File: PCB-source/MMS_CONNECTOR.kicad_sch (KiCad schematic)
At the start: 6 parts, among them J9 RJ45_LED_Shielded, U3 TPD2EUSB30DRTR-TP

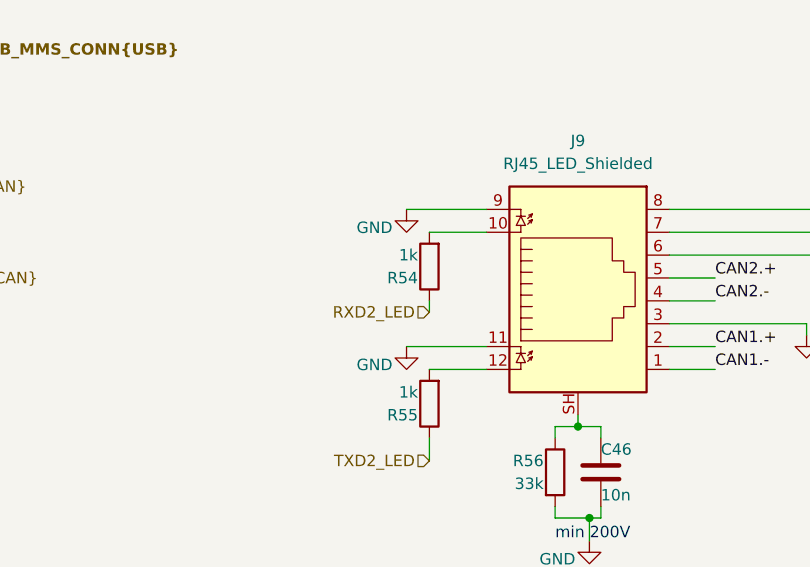
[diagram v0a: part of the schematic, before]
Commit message: change can term add usr led
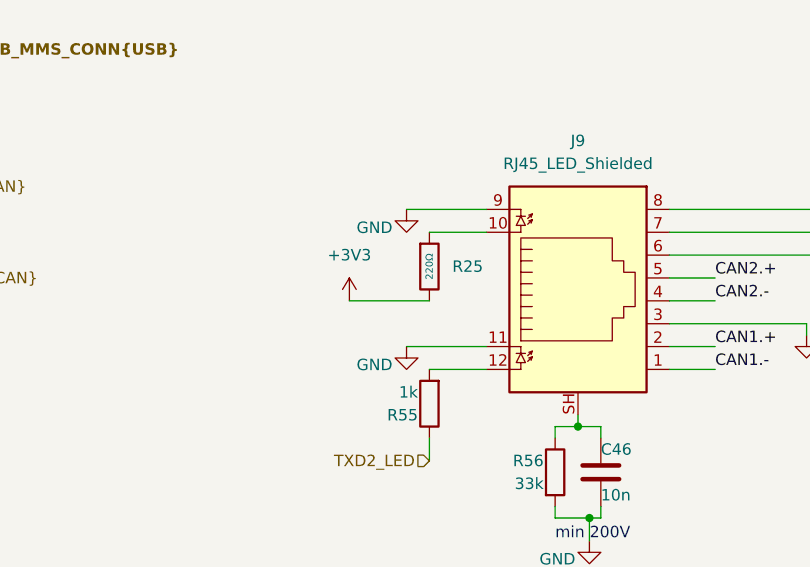
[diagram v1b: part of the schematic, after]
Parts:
- removed R54: 1k, Resistor_SMD:R_0402_1005Metric, symbol Device:R
- added R25: 220Ω, PCM_JLCPCB:R_0402, symbol PCM_JLCPCB-Resistors:0402,220Ω
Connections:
- net at J9.10: now also R25.1
- new net +3V3: R25.2

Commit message: DRC PASS, preparing bom for production
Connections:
- net +3V3 is gone; now on net TXD2_LED: R25.2
- net TXD2_LED: no longer R55.1
- new net RXD2_LED: R55.1
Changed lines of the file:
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@@
+	(wire
+		(pts
+			(xy 104.14 114.3) (xy 113.03 114.3)
+		)
+		(stroke
+			(width 0)
+			(type default)
+		)
+	)
 	(wire
 		(pts
@@
 			)
 			(justify left bottom)
-		)
-	)
-	(hierarchical_label "TXD2_LED"
-		(shape input)
-		(at 113.03 114.3 180)
-		(effects
-			(font
-				(size 1.27 1.27)
-			)
-			(justify right)
 		)
 	)
@@
 		)
 	)
+	(hierarchical_label "TXD2_LED"
+		(shape input)
+		(at 104.14 96.52 180)
+		(effects
+			(font
+				(size 1.27 1.27)
+			)
+			(justify right)
+		)
+	)
 	(hierarchical_label "CAN2{CAN}"
 		(shape bidirectional)
@@
 			)
 			(justify left)
+		)
+	)
+	(hierarchical_label "RXD2_LED"
+		(shape input)
+		(at 104.14 114.3 180)
+		(effects
+			(font
+				(size 1.27 1.27)
+			)
+			(justify right)
 		)
 	)
@@
 					(unit 1)
 				)
-			)
-		)
-	)
-	(symbol
-		(lib_id "power:+3V3")
-		(at 104.14 96.52 0)
-		(unit 1)
-		(exclude_from_sim no)
-		(in_bom yes)
-		(on_board yes)
-		(dnp no)
-		(fields_autoplaced yes)
-		(property "Reference" "#PWR084"
-			(at 104.14 100.33 0)
-			(effects
-				(font
-					(size 1.27 1.27)
-				)
-				(hide yes)
-			)
-		)
-		(property "Value" "+3V3"
-			(at 104.14 91.44 0)
-			(effects
-				(font
-					(size 1.27 1.27)
-				)
-			)
-		)
-		(property "Footprint" ""
-			(at 104.14 96.52 0)
-			(effects
-				(font
-					(size 1.27 1.27)
-				)
-				(hide yes)
-			)
-		)
-		(property "Datasheet" ""
-			(at 104.14 96.52 0)
-			(effects
-				(font
-					(size 1.27 1.27)
-				)
-				(hide yes)
-			)
-		)
-		(property "Description" "Power symbol creates a global label with name \"+3V3\""
-			(at 104.14 96.52 0)
-			(effects
-				(font
-					(size 1.27 1.27)
-				)
-				(hide yes)
-			)
-		)
-		(pin "1"
-		)
-		(instances
-			(project ""
-				(path "/6596548a-44e0-46d8-8624-fd71cf4a3e17/375a4799-1237-4cf9-80bd-b6d6bc52fffa"
-					(reference "#PWR085")
-					(unit 1)
-				)
-				(path "/6596548a-44e0-46d8-8624-fd71cf4a3e17/6dbf7263-2614-4625-a960-703f6ff0d778"
-					(reference "#PWR084")
-					(unit 1)
-				)

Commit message: bom done
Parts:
- removed C46: 10n, Capacitor_SMD:C_0402_1005Metric, symbol Device:C
- removed R55: 1k, Resistor_SMD:R_0402_1005Metric, symbol Device:R
- removed R56: 33k, Resistor_SMD:R_0402_1005Metric, symbol Device:R
- added C34: 10nF, PCM_JLCPCB:C_0402, symbol PCM_JLCPCB-Capacitors:0402,10nF
- added R27: 33kΩ, PCM_JLCPCB:R_0402, symbol PCM_JLCPCB-Resistors:0402,33kΩ
- added R6: 1kΩ, PCM_JLCPCB:R_0402, symbol PCM_JLCPCB-Resistors:0402,1kΩ
- J9: now left out of the parts list
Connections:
- net GND: now also C34.2, R27.2
- net RXD2_LED: now also R6.2
- net at J9.12: now also R6.1
- net at J9.SH: now also C34.1, R27.1

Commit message: REV A production ready
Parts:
- removed R6: 1kΩ, PCM_JLCPCB:R_0402, symbol PCM_JLCPCB-Resistors:0402,1kΩ
- added R6: 220Ω, PCM_JLCPCB:R_0402, symbol PCM_JLCPCB-Resistors:0402,220Ω
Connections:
- net RXD2_LED: now also R6.2
- net at J9.12: now also R6.1
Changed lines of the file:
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@@
+	)
+	(symbol
+		(lib_id "PCM_JLCPCB-Resistors:0402,220Ω")
+		(at 113.03 107.95 0)
+		(unit 1)
+		(exclude_from_sim no)
+		(in_bom yes)
+		(on_board yes)
+		(dnp no)
+		(property "Reference" "R6"
+			(at 114.554 107.95 0)
+			(effects
+				(font
+					(size 1.27 1.27)
+				)
+				(justify left)
+			)
+		)
+		(property "Value" "220Ω"
+			(at 113.03 107.95 90)
+			(do_not_autoplace yes)
+			(effects
+				(font
+					(size 0.8 0.8)
+				)
+			)
+		)
+		(property "Footprint" "PCM_JLCPCB:R_0402"
+			(at 111.252 107.95 90)
+			(effects
+				(font
+					(size 1.27 1.27)
+				)
+				(hide yes)
+			)
+		)
+		(property "Datasheet" "https://www.lcsc.com/datasheet/lcsc_datasheet_2205311900_UNI-ROYAL-Uniroyal-Elec-0402WGF2200TCE_C25091.pdf"
+			(at 113.03 107.95 0)
+			(effects
+				(font
+					(size 1.27 1.27)
+				)
+				(hide yes)
+			)
+		)
+		(property "Description" "62.5mW Thick Film Resistors 50V ±100ppm/°C ±1% 220Ω 0402 Chip Resistor - Surface Mount ROHS"
+			(at 113.03 107.95 0)
+			(effects
+				(font
+					(size 1.27 1.27)
+				)
+				(hide yes)
+			)
+		)
+		(property "LCSC" "C25091"
+			(at 113.03 107.95 0)
+			(effects
+				(font
+					(size 1.27 1.27)
+				)
+				(hide yes)
+			)
+		)
+		(property "Stock" "617243"
+			(at 113.03 107.95 0)
+			(effects
+				(font
+					(size 1.27 1.27)
+				)
+				(hide yes)
+			)
+		)
+		(property "Price" "0.004USD"
+			(at 113.03 107.95 0)
+			(effects
+				(font
+					(size 1.27 1.27)
+				)
+				(hide yes)
+			)
+		)
+		(property "Process" "SMT"
+			(at 113.03 107.95 0)
+			(effects
+				(font
+					(size 1.27 1.27)
+				)
+				(hide yes)
+			)
+		)
+		(property "Minimum Qty" "20"
+			(at 113.03 107.95 0)
+			(effects
+				(font
+					(size 1.27 1.27)
+				)
+				(hide yes)
+			)
+		)
+		(property "Attrition Qty" "10"
+			(at 113.03 107.95 0)
+			(effects
+				(font
+					(size 1.27 1.27)
+				)
+				(hide yes)
+			)
+		)
+		(property "Class" "Basic Component"
+			(at 113.03 107.95 0)
+			(effects
+				(font
+					(size 1.27 1.27)
+				)
+				(hide yes)
+			)
+		)
+		(property "Category" "Resistors,Chip Resistor - Surface Mount"
+			(at 113.03 107.95 0)
+			(effects
+				(font
+					(size 1.27 1.27)
+				)
+				(hide yes)
+			)
+		)
+		(property "Manufacturer" "UNI-ROYAL(Uniroyal Elec)"
+			(at 113.03 107.95 0)
+			(effects
+				(font
+					(size 1.27 1.27)
+				)
+				(hide yes)
+			)
+		)
+		(property "Part" "0402WGF2200TCE"
+			(at 113.03 107.95 0)
+			(effects
+				(font
+					(size 1.27 1.27)
+				)
+				(hide yes)
+			)
+		)
+		(property "Resistance" "220Ω"
+			(at 113.03 107.95 0)
+			(effects
+				(font
+					(size 1.27 1.27)
+				)
+				(hide yes)
+			)
+		)
+		(property "Power(Watts)" "62.5mW"
+			(at 113.03 107.95 0)
+			(effects
+				(font
+					(size 1.27 1.27)
+				)
+				(hide yes)
+			)
+		)
+		(property "Type" "Thick Film Resistors"
+			(at 113.03 107.95 0)
+			(effects
+				(font
+					(size 1.27 1.27)
+				)
+				(hide yes)
+			)
+		)
+		(property "Overload Voltage (Max)" "50V"
+			(at 113.03 107.95 0)
+			(effects
+				(font
+					(size 1.27 1.27)
+				)
+				(hide yes)
+			)
+		)
+		(property "Operating Temperature Range" "-55°C~+155°C"
+			(at 113.03 107.95 0)
+			(effects
+				(font
+					(size 1.27 1.27)
+				)
+				(hide yes)
+			)
+		)
+		(property "Tolerance" "±1%"
+			(at 113.03 107.95 0)
+			(effects
+				(font
+					(size 1.27 1.27)
+				)
+				(hide yes)
+			)
+		)
+		(property "Temperature Coefficient" "±100ppm/°C"
+			(at 113.03 107.95 0)
+			(effects
+				(font
+					(size 1.27 1.27)
+				)
+				(hide yes)
+			)
+		)
+		(pin "1"
+		)
+		(pin "2"
+		)
+		(instances
+			(project "MMS2"
+				(path "/6596548a-44e0-46d8-8624-fd71cf4a3e17/375a4799-1237-4cf9-80bd-b6d6bc52fffa"
+					(reference "R53")
+					(unit 1)
+				)
+				(path "/6596548a-44e0-46d8-8624-fd71cf4a3e17/6dbf7263-2614-4625-a960-703f6ff0d778"
+					(reference "R6")
+					(unit 1)
+				)
+			)
+		)
 	)
 	(symbol
@@
 					(unit 1)
 				)
-			)
-		)
-	)
-	(symbol
-		(lib_id "PCM_JLCPCB-Resistors:0402,1kΩ")
-		(at 113.03 107.95 0)
-		(unit 1)
-		(exclude_from_sim no)
-		(in_bom yes)
-		(on_board yes)
-		(dnp no)
-		(fields_autoplaced yes)
-		(property "Reference" "R6"
-			(at 115.57 107.9499 0)
-			(effects
-				(font
-					(size 1.27 1.27)
-				)
-				(justify left)
-			)
-		)
-		(property "Value" "1kΩ"
-			(at 113.03 107.95 90)
-			(do_not_autoplace yes)
-			(effects
-				(font
-					(size 0.8 0.8)
-				)
-			)
-		)
-		(property "Footprint" "PCM_JLCPCB:R_0402"
-			(at 111.252 107.95 90)
-			(effects
-				(font
-					(size 1.27 1.27)
-				)
-				(hide yes)
-			)
-		)
-		(property "Datasheet" "https://www.lcsc.com/datasheet/lcsc_datasheet_2206010216_UNI-ROYAL-Uniroyal-Elec-0402WGF1001TCE_C11702.pdf"
-			(at 113.03 107.95 0)
-			(effects
-				(font
-					(size 1.27 1.27)
-				)
-				(hide yes)
-			)
-		)
-		(property "Description" "62.5mW Thick Film Resistors 50V ±100ppm/°C ±1% 1kΩ 0402 Chip Resistor - Surface Mount ROHS"
-			(at 113.03 107.95 0)
-			(effects
-				(font
-					(size 1.27 1.27)
-				)
-				(hide yes)
-			)
-		)
-		(property "LCSC" "C11702"
-			(at 113.03 107.95 0)
-			(effects
-				(font
-					(size 1.27 1.27)
-				)
-				(hide yes)
-			)
-		)
-		(property "Stock" "6889074"
-			(at 113.03 107.95 0)
-			(effects
-				(font
-					(size 1.27 1.27)
-				)
-				(hide yes)
-			)
-		)
-		(property "Price" "0.004USD"
-			(at 113.03 107.95 0)
-			(effects
-				(font
-					(size 1.27 1.27)
-				)
-				(hide yes)
-			)
-		)
-		(property "Process" "SMT"
-			(at 113.03 107.95 0)
-			(effects
-				(font
-					(size 1.27 1.27)
-				)
-				(hide yes)
-			)
-		)
-		(property "Minimum Qty" "20"
-			(at 113.03 107.95 0)
-			(effects
-				(font
-					(size 1.27 1.27)
-				)
-				(hide yes)
-			)
-		)
-		(property "Attrition Qty" "10"
-			(at 113.03 107.95 0)
-			(effects
-				(font
-					(size 1.27 1.27)
-				)
-				(hide yes)
-			)
-		)
-		(property "Class" "Basic Component"
-			(at 113.03 107.95 0)
-			(effects
-				(font
-					(size 1.27 1.27)
-				)
-				(hide yes)
-			)
-		)
-		(property "Category" "Resistors,Chip Resistor - Surface Mount"
-			(at 113.03 107.95 0)
-			(effects
-				(font
-					(size 1.27 1.27)
-				)
-				(hide yes)
-			)
-		)
-		(property "Manufacturer" "UNI-ROYAL(Uniroyal Elec)"
-			(at 113.03 107.95 0)
-			(effects
-				(font
-					(size 1.27 1.27)
-				)
-				(hide yes)
-			)
-		)
-		(property "Part" "0402WGF1001TCE"
-			(at 113.03 107.95 0)
-			(effects
-				(font
-					(size 1.27 1.27)
-				)
-				(hide yes)
-			)
-		)
-		(property "Resistance" "1kΩ"
-			(at 113.03 107.95 0)
-			(effects
-				(font
-					(size 1.27 1.27)
-				)
-				(hide yes)
-			)
-		)
-		(property "Power(Watts)" "62.5mW"
-			(at 113.03 107.95 0)
-			(effects
-				(font
-					(size 1.27 1.27)
-				)
-				(hide yes)
-			)
-		)
-		(property "Type" "Thick Film Resistors"
-			(at 113.03 107.95 0)
-			(effects
-				(font
-					(size 1.27 1.27)
-				)
-				(hide yes)
-			)
-		)
-		(property "Overload Voltage (Max)" "50V"
-			(at 113.03 107.95 0)
-			(effects
-				(font
-					(size 1.27 1.27)
-				)
-				(hide yes)
-			)
-		)
-		(property "Operating Temperature Range" "-55°C~+155°C"
-			(at 113.03 107.95 0)
-			(effects
-				(font
-					(size 1.27 1.27)
-				)
-				(hide yes)
-			)
-		)
-		(property "Tolerance" "±1%"
-			(at 113.03 107.95 0)
-			(effects
-				(font
-					(size 1.27 1.27)
-				)
-				(hide yes)
-			)
-		)
-		(property "Temperature Coefficient" "±100ppm/°C"
-			(at 113.03 107.95 0)
-			(effects
-				(font
-					(size 1.27 1.27)
-				)
-				(hide yes)
-			)
-		)
-		(pin "2"
-		)
-		(pin "1"
-		)
-		(instances
-			(project ""
-				(path "/6596548a-44e0-46d8-8624-fd71cf4a3e17/375a4799-1237-4cf9-80bd-b6d6bc52fffa"
-					(reference "R53")
-					(unit 1)
-				)
-				(path "/6596548a-44e0-46d8-8624-fd71cf4a3e17/6dbf7263-2614-4625-a960-703f6ff0d778"
-					(reference "R6")
-					(unit 1)
-				)
